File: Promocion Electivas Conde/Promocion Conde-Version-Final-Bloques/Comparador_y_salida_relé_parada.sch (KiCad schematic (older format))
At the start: 23 parts, among them K1 DIPxx-1Cxx-51x, Q2 BC848, U5 TL082

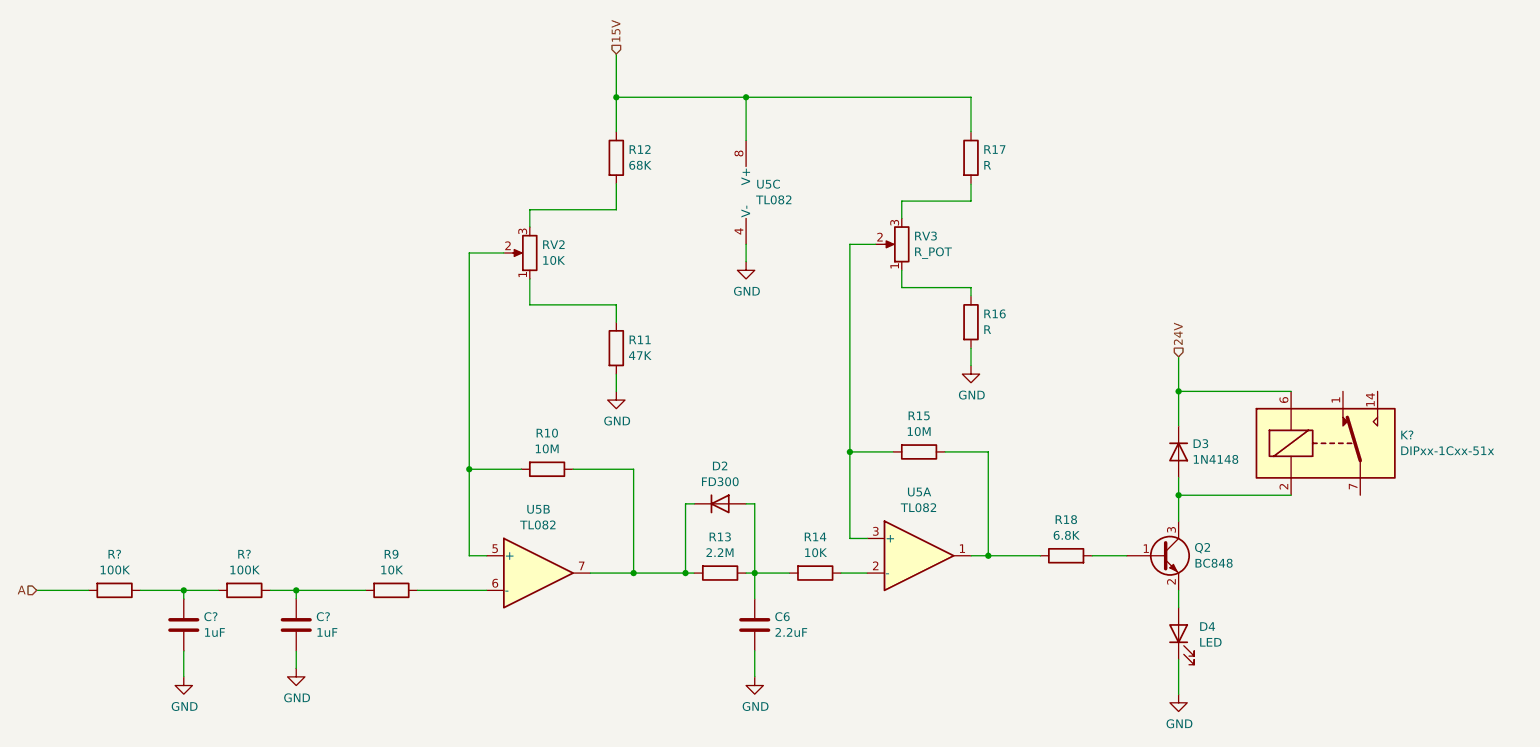
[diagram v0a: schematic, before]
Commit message: Bloques y footprint asignados
Falta elegir y asignar el de los potenciometros Rv3 y Rv7.
Las salidas K3 y K20 también...
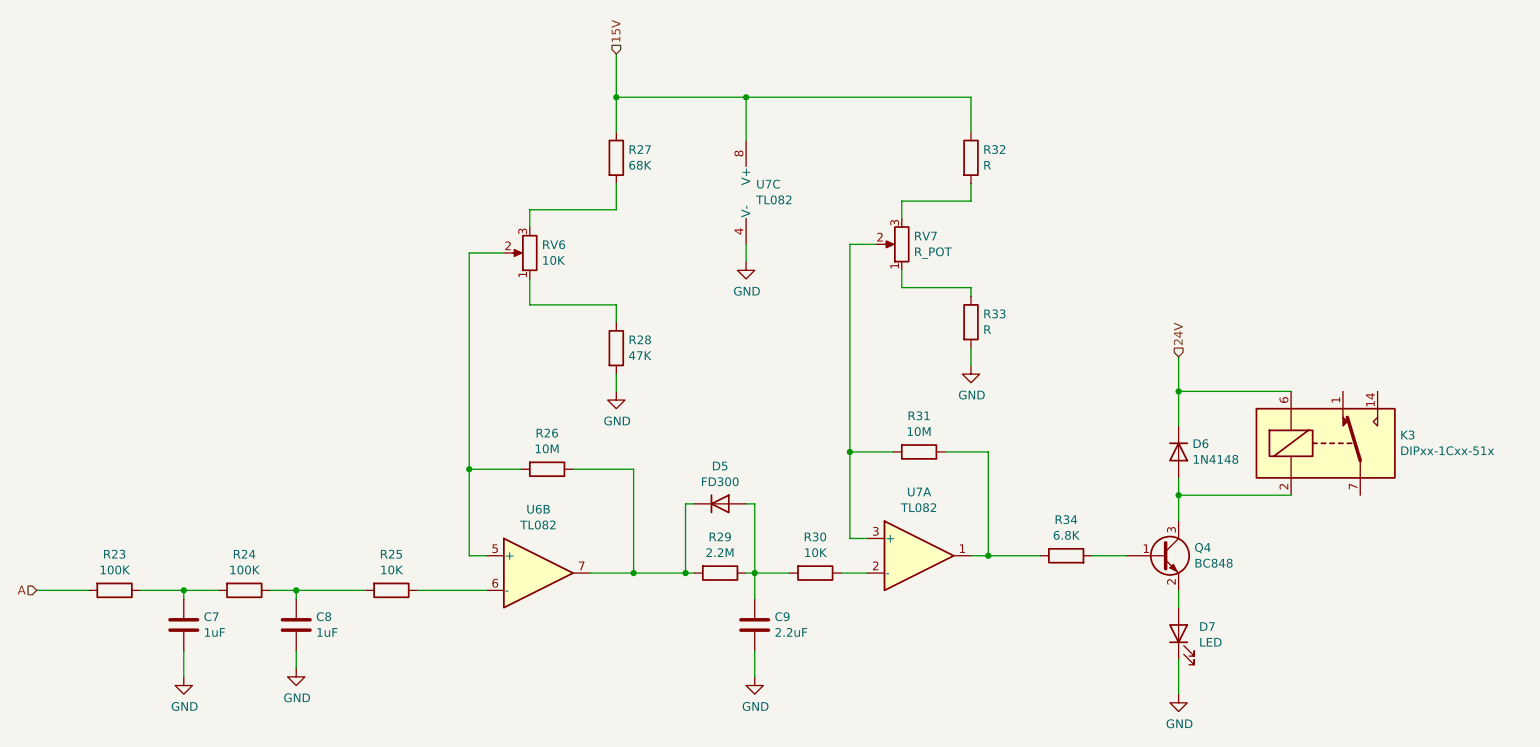
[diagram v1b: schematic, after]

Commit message: cambios salida a rele
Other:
- moved on the sheet: U7C
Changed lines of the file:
@@
-	1    0    0    -1
-$EndComp
-$Comp
-L Amplifier_Operational:TL082 U5
-U 2 1 61344A8C
-P 3700 4450
-AR Path="/61322896/61344A8C" Ref="U5"  Part="2"
-AR Path="/612F0357/61344A8C" Ref="U?"  Part="2"
-AR Path="/618B3478/61344A8C" Ref="U?"  Part="2"
-AR Path="/618B375A/61344A8C" Ref="U6"  Part="2"
-F 0 "U6" H 3700 4817 50  0000 C CNN
-F 1 "TL082" H 3700 4726 50  0000 C CNN
-F 2 "Package_SO:SOIC-8-1EP_3.9x4.9mm_P1.27mm_EP2.29x3mm" H 3700 4450 50  0001 C CNN
-F 3 "https://www.digikey.com/es/products/detail/texas-instruments/TL082CDE4/13472954" H 3700 4450 50  0001 C CNN
-	2    3700 4450
 	1    0    0    -1
 $EndComp
@@
 	4150 1450 4150 1700
 Wire Wire Line
-	4150 1700 4900 1700
-Wire Wire Line
 	6200 1700 6200 1900
 Connection ~ 4150 1700
@@
 Wire Wire Line
 	4950 5050 4950 4900
-$Comp
-L Amplifier_Operational:TL082 U5
-U 3 1 618C6FB1
-P 5000 2250
-AR Path="/61322896/618C6FB1" Ref="U5"  Part="3"
-AR Path="/612F0357/618C6FB1" Ref="U?"  Part="3"
-AR Path="/618B3478/618C6FB1" Ref="U?"  Part="3"
-AR Path="/618B375A/618C6FB1" Ref="U7"  Part="3"
-F 0 "U7" H 4958 2296 50  0000 L CNN
-F 1 "TL082" H 4958 2205 50  0000 L CNN
-F 2 "Package_SO:SOIC-8-1EP_3.9x4.9mm_P1.27mm_EP2.29x3mm" H 5000 2250 50  0001 C CNN
-F 3 "https://www.digikey.com/es/products/detail/texas-instruments/TL082CDE4/13472954" H 5000 2250 50  0001 C CNN
-	3    5000 2250
-	1    0    0    -1
-$EndComp
-Wire Wire Line
-	4900 1950 4900 1700
-Connection ~ 4900 1700
-Wire Wire Line
-	4900 1700 6200 1700
-$Comp
-L power:GND #PWR0121
-U 1 1 618C6FB2
-P 4900 2650
-AR Path="/61322896/618C6FB2" Ref="#PWR0121"  Part="1"
-AR Path="/612F0357/618C6FB2" Ref="#PWR?"  Part="1"
-AR Path="/618B3478/618C6FB2" Ref="#PWR?"  Part="1"
-AR Path="/618B375A/618C6FB2" Ref="#PWR0129"  Part="1"
-F 0 "#PWR0129" H 4900 2400 50  0001 C CNN
-F 1 "GND" H 4905 2477 50  0000 C CNN
-F 2 "" H 4900 2650 50  0001 C CNN
-F 3 "" H 4900 2650 50  0001 C CNN
-	1    4900 2650
-	1    0    0    -1
-$EndComp
-Wire Wire Line
-	4900 2650 4900 2550
 $Comp
 L Device:R R18
@@
 Wire Wire Line
 	7400 4000 7400 3900
+Wire Wire Line
+	4150 1700 4500 1700
+$Comp
+L Amplifier_Operational:TL082 U5
+U 2 1 61344A8C
+P 3700 4450
+AR Path="/61322896/61344A8C" Ref="U5"  Part="2"
+AR Path="/612F0357/61344A8C" Ref="U?"  Part="2"
+AR Path="/618B3478/61344A8C" Ref="U?"  Part="2"
+AR Path="/618B375A/61344A8C" Ref="U6"  Part="2"
+F 0 "U6" H 3550 4800 50  0000 C CNN
+F 1 "TL082" H 3600 4700 50  0000 C CNN
+F 2 "Package_SO:SOIC-8-1EP_3.9x4.9mm_P1.27mm_EP2.29x3mm" H 3700 4450 50  0001 C CNN
+F 3 "https://www.digikey.com/es/products/detail/texas-instruments/TL082CDE4/13472954" H 3700 4450 50  0001 C CNN
+	2    3700 4450
+	1    0    0    -1
+$EndComp
+Wire Wire Line
+	3800 4850 3800 4750
+$Comp
+L power:GND #PWR0121
+U 1 1 618C6FB2
+P 3800 4850
+AR Path="/61322896/618C6FB2" Ref="#PWR0121"  Part="1"
+AR Path="/612F0357/618C6FB2" Ref="#PWR?"  Part="1"
+AR Path="/618B3478/618C6FB2" Ref="#PWR?"  Part="1"
+AR Path="/618B375A/618C6FB2" Ref="#PWR0129"  Part="1"
+F 0 "#PWR0129" H 3800 4600 50  0001 C CNN
+F 1 "GND" H 3805 4677 50  0000 C CNN
+F 2 "" H 3800 4850 50  0001 C CNN
+F 3 "" H 3800 4850 50  0001 C CNN
+	1    3800 4850
+	1    0    0    -1
+$EndComp
+$Comp
+L Amplifier_Operational:TL082 U5
+U 3 1 618C6FB1
+P 3900 4450
+AR Path="/61322896/618C6FB1" Ref="U5"  Part="3"
+AR Path="/612F0357/618C6FB1" Ref="U?"  Part="3"
+AR Path="/618B3478/618C6FB1" Ref="U?"  Part="3"
+AR Path="/618B375A/618C6FB1" Ref="U7"  Part="3"
+F 0 "U7" H 3900 4650 50  0000 L CNN
+F 1 "TL082" H 3900 4750 50  0000 L CNN
+F 2 "Package_SO:SOIC-8-1EP_3.9x4.9mm_P1.27mm_EP2.29x3mm" H 3900 4450 50  0001 C CNN
+F 3 "https://www.digikey.com/es/products/detail/texas-instruments/TL082CDE4/13472954" H 3900 4450 50  0001 C CNN
+	3    3900 4450
+	1    0    0    -1
+$EndComp
+Wire Wire Line
+	3800 4150 3800 4000
+Wire Wire Line
+	4500 4000 4500 1700
+Wire Wire Line
+	3800 4000 4500 4000
+Connection ~ 4500 1700
+Wire Wire Line
+	4500 1700 6200 1700
 $EndSCHEMATC

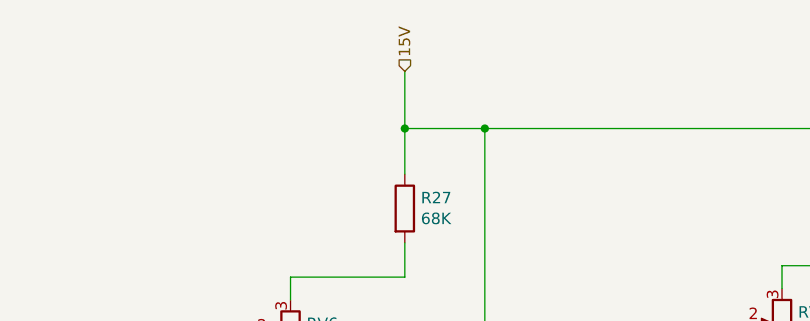
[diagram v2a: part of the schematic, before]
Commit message: Actualizacion Convertidor
Se creó el esquemático del convertidor y se hizo la conexión del mismo
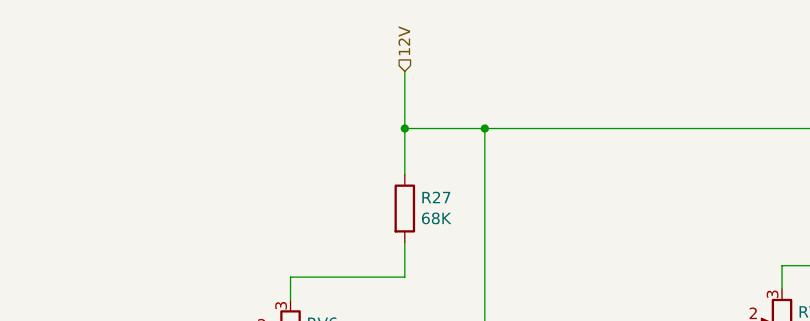
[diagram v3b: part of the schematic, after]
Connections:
- net 15V renamed 12V
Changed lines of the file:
@@
 	4150 3400 4150 3300
 Text HLabel 4150 1450 1    50   Input ~ 0
-15V
+12V
 $Comp
 L Device:R R13

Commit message: Actualizacion
Actualizo los footprints del esquematico y se inicia el PCB
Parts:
- D3: footprint Diode_THT:D_DO-35_SOD27_P7.62mm_Horizontal -> Diode_SMD:D_SOD-323
- D4: footprint Diode_SMD:D_0603_1608Metric_Pad1.05x0.95mm_HandSolder -> LED_SMD:LED_1206_3216Metric
- RV2: footprint Resistor_SMD:R_0603_1608Metric_Pad0.98x0.95mm_HandSolder -> Potentiometer_SMD:Potentiometer_Vishay_TS53YL_Vertical
- RV3: footprint (none) -> Potentiometer_SMD:Potentiometer_Vishay_TS53YL_Vertical
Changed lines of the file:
@@
 F 0 "RV6" H 3580 2554 50  0000 R CNN
 F 1 "10K" H 3580 2645 50  0000 R CNN
-F 2 "Resistor_SMD:R_0603_1608Metric_Pad0.98x0.95mm_HandSolder" H 3650 2600 50  0001 C CNN
-F 3 "~" H 3650 2600 50  0001 C CNN
+F 2 "Potentiometer_SMD:Potentiometer_Vishay_TS53YL_Vertical" H 3650 2600 50  0001 C CNN
+F 3 "https://www.vishay.com/docs/51008/ts53.pdf" H 3650 2600 50  0001 C CNN
 	1    3650 2600
 	-1   0    0    1
@@
 F 0 "RV7" H 5730 2504 50  0000 R CNN
 F 1 "R_POT" H 5730 2595 50  0000 R CNN
-F 2 "" H 5800 2550 50  0001 C CNN
-F 3 "~" H 5800 2550 50  0001 C CNN
+F 2 "Potentiometer_SMD:Potentiometer_Vishay_TS53YL_Vertical" H 5800 2550 50  0001 C CNN
+F 3 "https://www.vishay.com/docs/51008/ts53.pdf" H 5800 2550 50  0001 C CNN
 	1    5800 2550
 	-1   0    0    1
@@
 F 0 "D7" V 7439 4682 50  0000 R CNN
 F 1 "LED" V 7348 4682 50  0000 R CNN
-F 2 "Diode_SMD:D_0603_1608Metric_Pad1.05x0.95mm_HandSolder" H 7400 4800 50  0001 C CNN
-F 3 "~" H 7400 4800 50  0001 C CNN
+F 2 "LED_SMD:LED_1206_3216Metric" H 7400 4800 50  0001 C CNN
+F 3 "https://www.aopled.com/AOP_PDFs/L152L-LIC.pdf" H 7400 4800 50  0001 C CNN
 	1    7400 4800
 	0    -1   -1   0
@@
 F 0 "D6" V 7354 3830 50  0000 L CNN
 F 1 "1N4148" V 7445 3830 50  0000 L CNN
-F 2 "Diode_THT:D_DO-35_SOD27_P7.62mm_Horizontal" H 7400 3575 50  0001 C CNN
-F 3 "https://assets.nexperia.com/documents/data-sheet/1N4148_1N4448.pdf" H 7400 3750 50  0001 C CNN
+F 2 "Diode_SMD:D_SOD-323" H 7400 3575 50  0001 C CNN
+F 3 "https://www.diodes.com/assets/Datasheets/1N4148WSF.pdf" H 7400 3750 50  0001 C CNN
 	1    7400 3750
 	0    1    1    0
